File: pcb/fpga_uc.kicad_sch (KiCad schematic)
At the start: 11 parts

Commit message: add missing values again
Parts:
- C?: value (none) -> 100u
- J?: value (none) -> FPGA_JTAG; footprint (none) -> Connector_PinHeader_2.54mm:PinHeader_2x07_P2.54mm_Vertical_SMD
- R? (x2): value (none) -> 4.7k; footprint (none) -> Resistor_SMD:R_2512_6332Metric_Pad1.40x3.35mm_HandSolder
- R?: value (none) -> 2.4k; footprint (none) -> Resistor_SMD:R_2512_6332Metric_Pad1.40x3.35mm_HandSolder
- U?: value (none) -> S25FL127SABMFV101; footprint (none) -> SOC008_SPA
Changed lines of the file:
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@@
       (effects (font (size 1.27 1.27)) hide)
     )
-    (property "Value" "" (id 1) (at 236.22 77.47 0))
+    (property "Value" "+3V3" (id 1) (at 236.22 77.47 0))
     (property "Footprint" "" (id 2) (at 236.22 82.55 0)
       (effects (font (size 1.27 1.27)) hide)
@@
     (in_bom yes) (on_board yes)
     (property "Reference" "R?" (id 0) (at 228.6 86.36 90))
-    (property "Value" "" (id 1) (at 231.14 86.36 90))
-    (property "Footprint" "" (id 2) (at 232.918 86.36 90)
+    (property "Value" "4.7k" (id 1) (at 231.14 86.36 90))
+    (property "Footprint" "Resistor_SMD:R_2512_6332Metric_Pad1.40x3.35mm_HandSolder" (id 2) (at 232.918 86.36 90)
       (effects (font (size 1.27 1.27)) hide)
     )
@@
       (effects (font (size 1.27 1.27)) hide)
     )
-    (property "Value" "" (id 1) (at 124.46 74.9299 0)
+    (property "Value" "GND" (id 1) (at 124.46 74.9299 0)
       (effects (font (size 1.27 1.27)) (justify left))
     )
@@
       (effects (font (size 1.27 1.27)) hide)
     )
-    (property "Value" "" (id 1) (at 231.14 113.03 0))
+    (property "Value" "+3.3V" (id 1) (at 231.14 113.03 0))
     (property "Footprint" "" (id 2) (at 236.22 114.3 0)
       (effects (font (size 1.27 1.27)) hide)
@@
       (effects (font (size 1.27 1.27)) hide)
     )
-    (property "Value" "" (id 1) (at 227.33 120.65 0))
+    (property "Value" "GND" (id 1) (at 227.33 120.65 0))
     (property "Footprint" "" (id 2) (at 231.14 119.38 0)
       (effects (font (size 1.27 1.27)) hide)
@@
     (in_bom yes) (on_board yes)
     (property "Reference" "R?" (id 0) (at 215.9 86.36 90))
-    (property "Value" "" (id 1) (at 218.44 86.36 90))
-    (property "Footprint" "" (id 2) (at 216.662 86.36 90)
+    (property "Value" "2.4k" (id 1) (at 218.44 86.36 90))
+    (property "Footprint" "Resistor_SMD:R_2512_6332Metric_Pad1.40x3.35mm_HandSolder" (id 2) (at 216.662 86.36 90)
       (effects (font (size 1.27 1.27)) hide)
     )
@@
     (in_bom yes) (on_board yes)
     (property "Reference" "R?" (id 0) (at 222.25 86.36 90))
-    (property "Value" "" (id 1) (at 224.79 86.36 90))
-    (property "Footprint" "" (id 2) (at 226.568 86.36 90)
+    (property "Value" "4.7k" (id 1) (at 224.79 86.36 90))
+    (property "Footprint" "Resistor_SMD:R_2512_6332Metric_Pad1.40x3.35mm_HandSolder" (id 2) (at 226.568 86.36 90)
       (effects (font (size 1.27 1.27)) hide)
     )
@@
     (in_bom yes) (on_board yes) (fields_autoplaced)
     (property "Reference" "J?" (id 0) (at 128.27 49.53 0))
-    (property "Value" "" (id 1) (at 128.27 52.07 0))
-    (property "Footprint" "" (id 2) (at 127 63.5 0)
+    (property "Value" "FPGA_JTAG" (id 1) (at 128.27 52.07 0))
+    (property "Footprint" "Connector_PinHeader_2.54mm:PinHeader_2x07_P2.54mm_Vertical_SMD" (id 2) (at 127 63.5 0)
       (effects (font (size 1.27 1.27)) hide)
     )
@@
       (effects (font (size 1.524 1.524)) (justify left))
     )
-    (property "Value" "" (id 1) (at 243.84 83.82 0)
+    (property "Value" "S25FL127SABMFV101" (id 1) (at 243.84 83.82 0)
       (effects (font (size 1.524 1.524)) (justify left))
     )
-    (property "Footprint" "" (id 2) (at 256.54 85.344 0)
+    (property "Footprint" "SOC008_SPA" (id 2) (at 256.54 85.344 0)
       (effects (font (size 1.524 1.524)) hide)
     )
@@
       (effects (font (size 1.27 1.27)) (justify left))
     )
-    (property "Value" "" (id 1) (at 215.9 114.2999 0)
+    (property "Value" "100u" (id 1) (at 215.9 114.2999 0)
       (effects (font (size 1.27 1.27)) (justify left))
     )
@@
       (effects (font (size 1.27 1.27)) hide)
     )
-    (property "Value" "" (id 1) (at 138.43 50.8 0))
+    (property "Value" "+3V3" (id 1) (at 138.43 50.8 0))
     (property "Footprint" "" (id 2) (at 138.43 55.88 0)
       (effects (font (size 1.27 1.27)) hide)

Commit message: commit before merge
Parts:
- added R? (x2): 10k, symbol Device:R
- R?: value ~ -> 330
- R? (x2): value ~ -> 4.7k
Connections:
- net +3V3: now also R?.1, R?.1
- net DONE: no longer R?.2, U?.L9 (PROGRAM_B_0)
- net at J?.6 (Pin_6), U?.L7 (TCK_0): now also R?.2
- net at J?.4 (Pin_4), U?.M7 (TMS_0): now also R?.2
- new net PROGRAM_B: R?.2, U?.L9 (PROGRAM_B_0)
- no-connect marks 2 -> 4
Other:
- moved on the sheet: C?, R?, U?

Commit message: maybe finished schematic
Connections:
- net +3.3V: now also C?.1, J?.2 (Pin_2), R?.1, R?.1, R?.1, R?.2, R?.2, U?.M9 (M0_0)
- net +3V3: no longer C?.1, J?.2 (Pin_2), R?.1, R?.1, R?.1, R?.2, R?.2, U?.M9 (M0_0)
- net DONE renamed FPGA_DONE
- net PROGRAM_B renamed FPGA_PROGRAM_B

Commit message: add footprints
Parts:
- C1401: renamed from C?; value ~ -> 47u; footprint (none) -> Capacitor_SMD:C_0805_2012Metric_Pad1.18x1.45mm_HandSolder
- C1402: renamed from C?; footprint (none) -> Capacitor_SMD:C_1210_3225Metric_Pad1.33x2.70mm_HandSolder
- R1401, R1402, R1403, R1404, R1405: renamed from R?; footprint (none) -> Resistor_SMD:R_0805_2012Metric_Pad1.20x1.40mm_HandSolder
- R1406, R1407, R1408: renamed from R?; footprint Resistor_SMD:R_2512_6332Metric_Pad1.40x3.35mm_HandSolder -> Resistor_SMD:R_0805_2012Metric_Pad1.20x1.40mm_HandSolder
- U1401: renamed from U?; footprint (none) -> fpga:BGA256C100P16X16_1700X1700X155
- gave numbers to parts that had none: 2
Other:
- moved on the sheet: C1401

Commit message: start layout
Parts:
- removed U1401: ~, fpga:BGA256C100P16X16_1700X1700X155, symbol FPGA_Xilinx_Artix7:XC7A100T-FTG256
- added U666: XC7A75T-FTG256, Package_BGA:Xilinx_FTG256, symbol FPGA_Xilinx_Artix7:XC7A75T-FTG256
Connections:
- net +3.3V: now also U666.M9 (M0_0)
- net +3V3: now also U666.E7 (CFGBVS_0), U666.L6 (VCCO_0)
- net FPGA_DONE: now also U666.H10 (DONE_0)
- net FPGA_PROGRAM_B: now also U666.L9 (PROGRAM_B_0)
- net GND: now also U666.H7 (VREFN_0), U666.H8 (VP_0), U666.J7 (VN_0), U666.J8 (VREFP_0), U666.M10 (M1_0), U666.M11 (M2_0)
- net at U1402.6 (CLK): now also U666.E8 (CCLK_0)
- net at R1402.2: now also U666.K10 (INIT_B_0)
- net at J1401.6 (Pin_6), R1405.2: now also U666.L7 (TCK_0)
- net at J1401.4 (Pin_4), R1404.2: now also U666.M7 (TMS_0)
- net at J1401.10 (Pin_10): now also U666.N7 (TDI_0)
- net at J1401.8 (Pin_8): now also U666.N8 (TDO_0)

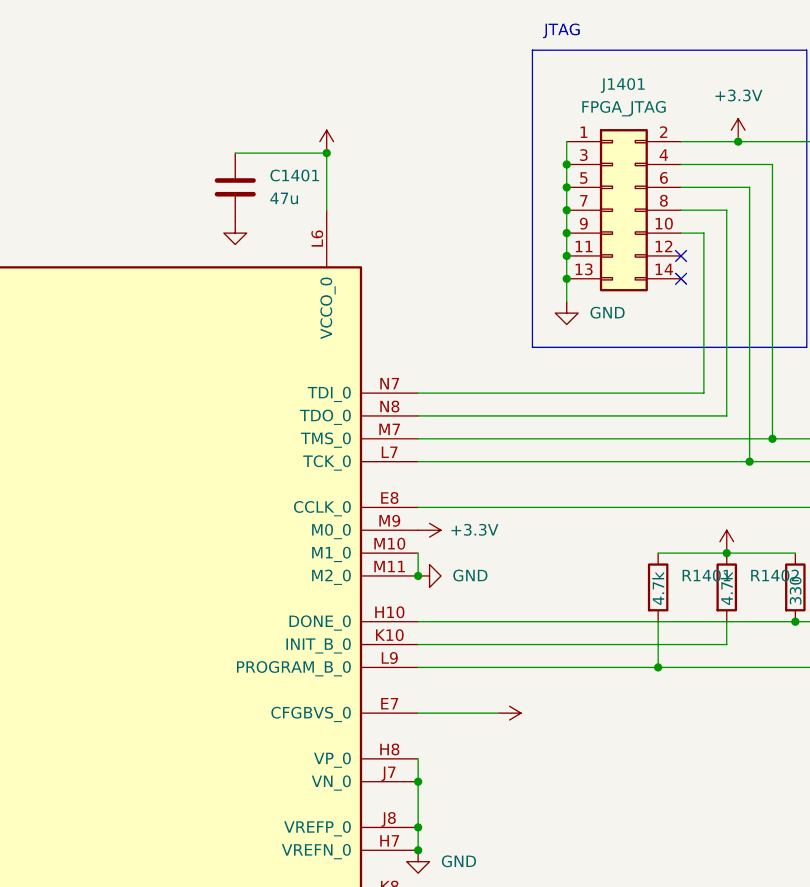
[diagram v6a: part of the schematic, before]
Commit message: connect onboard controller
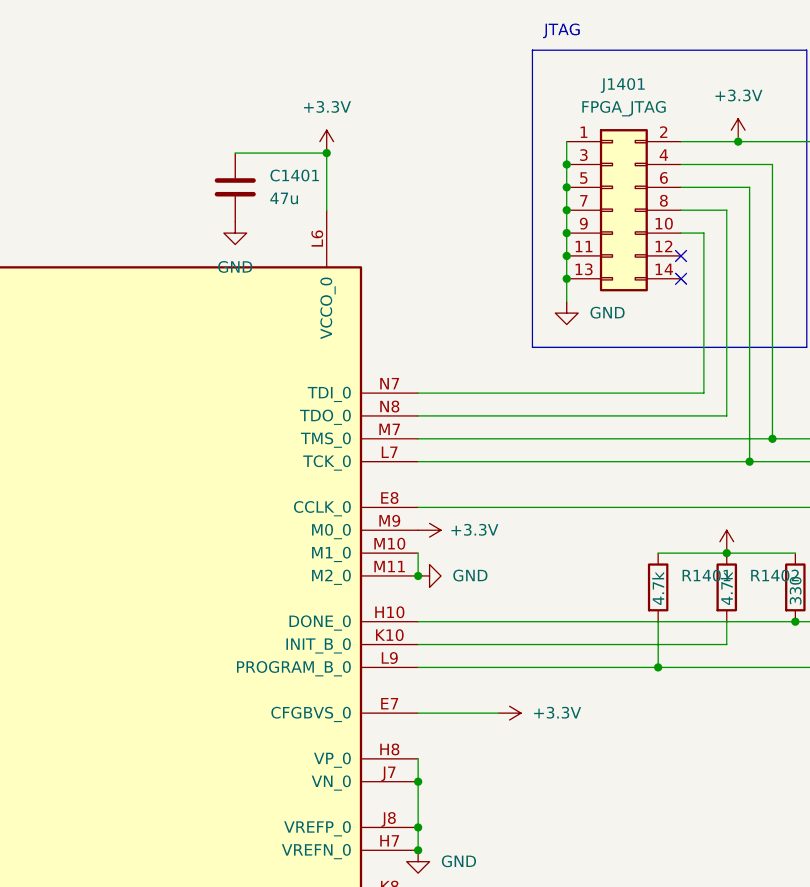
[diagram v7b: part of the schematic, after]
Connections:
- net +3.3V: now also C1401.1, U666.E7 (CFGBVS_0), U666.L6 (VCCO_0)
- net +3V3: no longer C1401.1, U666.E7 (CFGBVS_0), U666.L6 (VCCO_0)
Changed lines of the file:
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@@
   (junction (at 121.92 68.58) (diameter 0) (color 0 0 0 0)
   )
+  (junction (at 95.25 57.15) (diameter 0) (color 0 0 0 0)
+  )
   (junction (at 105.41 134.62) (diameter 0) (color 0 0 0 0)
   )
@@
   )
   (junction (at 140.97 55.88) (diameter 0) (color 0 0 0 0)
-  )
-  (junction (at 95.25 57.15) (diameter 0) (color 0 0 0 0)
   )
   (junction (at 218.44 85.09) (diameter 0) (color 0 0 0 0)
@@
     (pin "1")
   )
-  (symbol (lib_id "power:GND") (at 85.09 64.77 0) (unit 1)
-    (in_bom yes) (on_board yes) (fields_autoplaced)
-    (property "Reference" "#PWR01401" (id 0) (at 85.09 71.12 0)
-      (effects (font (size 1.27 1.27)) hide)
-    )
-    (property "Value" "~" (id 1) (at 85.09 69.85 0))
-    (property "Footprint" "" (id 2) (at 85.09 64.77 0)
-      (effects (font (size 1.27 1.27)) hide)
-    )
-    (property "Datasheet" "" (id 3) (at 85.09 64.77 0)
-      (effects (font (size 1.27 1.27)) hide)
-    )
-    (pin "1")
-  )
   (symbol (lib_id "power:+3.3V") (at 140.97 55.88 0) (unit 1)
     (in_bom yes) (on_board yes) (fields_autoplaced)
@@
     (pin "1")
   )
+  (symbol (lib_id "power:+3.3V") (at 114.3 119.38 270) (unit 1)
+    (in_bom yes) (on_board yes) (fields_autoplaced)
+    (property "Reference" "#PWR0106" (id 0) (at 110.49 119.38 0)
+      (effects (font (size 1.27 1.27)) hide)
+    )
+    (property "Value" "+3.3V" (id 1) (at 118.11 119.3799 90)
+      (effects (font (size 1.27 1.27)) (justify left))
+    )
+    (property "Footprint" "" (id 2) (at 114.3 119.38 0)
+      (effects (font (size 1.27 1.27)) hide)
+    )
+    (property "Datasheet" "" (id 3) (at 114.3 119.38 0)
+      (effects (font (size 1.27 1.27)) hide)
+    )
+    (pin "1")
+  )
   (symbol (lib_id "Device:R") (at 139.7 105.41 0) (unit 1)
     (in_bom yes) (on_board yes)
@@
     (pin "1")
   )
-  (symbol (lib_id "power:+3V3") (at 114.3 119.38 270) (unit 1)
-    (in_bom yes) (on_board yes) (fields_autoplaced)
-    (property "Reference" "#PWR01406" (id 0) (at 110.49 119.38 0)
-      (effects (font (size 1.27 1.27)) hide)
-    )
-    (property "Value" "~" (id 1) (at 118.11 119.3799 90)
-      (effects (font (size 1.27 1.27)) (justify left))
-    )
-    (property "Footprint" "" (id 2) (at 114.3 119.38 0)
-      (effects (font (size 1.27 1.27)) hide)
-    )
-    (property "Datasheet" "" (id 3) (at 114.3 119.38 0)
-      (effects (font (size 1.27 1.27)) hide)
-    )
-    (pin "1")
-  )
   (symbol (lib_id "Device:C") (at 85.09 60.96 0) (unit 1)
     (in_bom yes) (on_board yes) (fields_autoplaced)
@@
     (pin "2")
   )
-  (symbol (lib_id "power:+3V3") (at 95.25 57.15 0) (unit 1)
-    (in_bom yes) (on_board yes) (fields_autoplaced)
-    (property "Reference" "#PWR01402" (id 0) (at 95.25 60.96 0)
-      (effects (font (size 1.27 1.27)) hide)
-    )
-    (property "Value" "~" (id 1) (at 95.25 52.07 0))
+  (symbol (lib_id "power:+3.3V") (at 95.25 57.15 0) (unit 1)
+    (in_bom yes) (on_board yes) (fields_autoplaced)
+    (property "Reference" "#PWR0107" (id 0) (at 95.25 60.96 0)
+      (effects (font (size 1.27 1.27)) hide)
+    )
+    (property "Value" "+3.3V" (id 1) (at 95.25 52.07 0))
     (property "Footprint" "" (id 2) (at 95.25 57.15 0)
       (effects (font (size 1.27 1.27)) hide)
@@
       (effects (font (size 1.27 1.27)) hide)
     )
+    (pin "1")
+  )
+  (symbol (lib_id "power:GND") (at 85.09 64.77 0) (unit 1)
+    (in_bom yes) (on_board yes) (fields_autoplaced)
+    (property "Reference" "#PWR0108" (id 0) (at 85.09 71.12 0)
+      (effects (font (size 1.27 1.27)) hide)
+    )
+    (property "Value" "GND" (id 1) (at 85.09 69.85 0))
+    (property "Footprint" "" (id 2) (at 85.09 64.77 0)
+      (effects (font (size 1.27 1.27)) hide)
+    )
+    (property "Datasheet" "" (id 3) (at 85.09 64.77 0)
+      (effects (font (size 1.27 1.27)) hide)
+    )

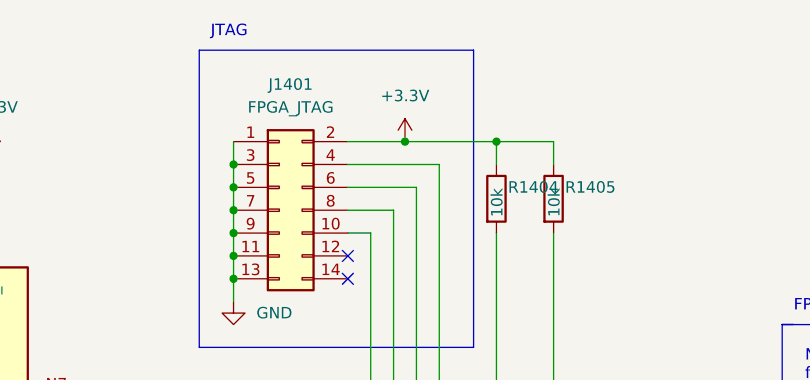
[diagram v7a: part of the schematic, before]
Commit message: change footprint of debug_connector
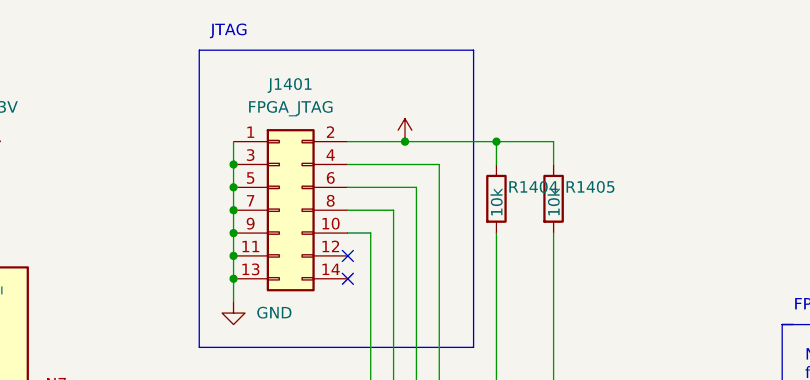
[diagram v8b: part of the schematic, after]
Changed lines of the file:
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@@
       (effects (font (size 1.27 1.27)) hide)
     )
-    (property "Value" "+3.3V" (id 1) (at 140.97 50.8 0))
+    (property "Value" "" (id 1) (at 140.97 50.8 0))
     (property "Footprint" "" (id 2) (at 140.97 55.88 0)
       (effects (font (size 1.27 1.27)) hide)
